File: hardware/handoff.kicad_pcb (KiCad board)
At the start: 2 copper layers, 40 x 62 mm, 65 parts, among them J1 BAT XH-2, J2 PAD JST-XH 2p, J3 LED JST-XH 4p / 5mm RGB, J5 CHG XH-2, J6 MOT 1x02 2.54, Q1 AO3400A, SW1 SS-12F23G5, SW2 TACT 6x6, U1 Raspberry Pi Pico 2 W, U2 MCP6292-E/MS

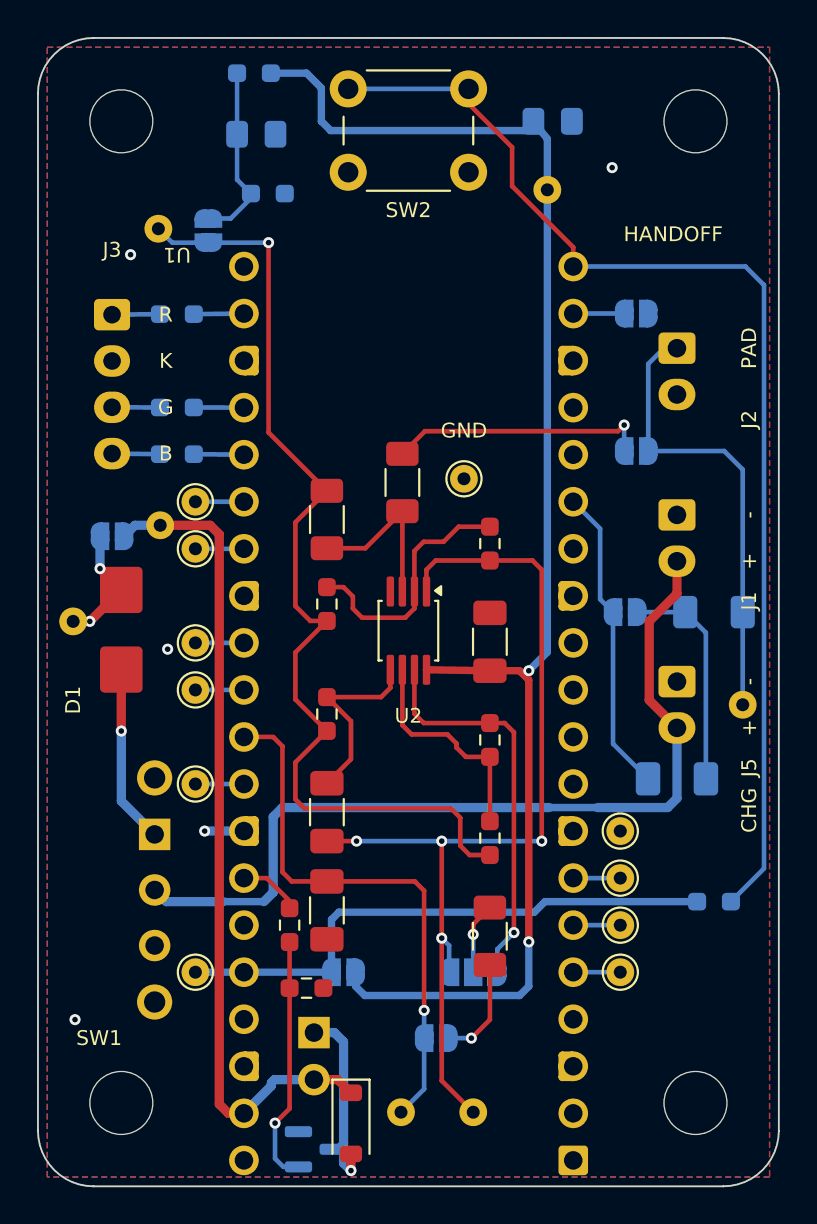
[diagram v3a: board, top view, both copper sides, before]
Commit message: Remove E1-E10, shrink the boss to 6 mm, and untangle the elbow
The board came in with 51 DRC errors. The previous session had been asked to
move D3 to the SS220F (SMB) like D1, and there was nowhere to put it: the SMB
took TP2 and TP3's spot beside J6, TP2 and TP3 were pushed out through two
gaps in the Pico's pin row to the little-finger wall, and there they landed on
top of the breakout pads. Four vias and two shorted pads to make room for one
diode. Take the space back instead of routing round the lack of it.

E1-E10 go. Ten through-hole pads on nets nothing uses, a column down each
wall, three of them (GP0, GP1, GND) sitting inside H4's boss for three
sessions. Gone from the schematic, the board, the DRU rule and the parts
list; the eight Pico pins they broke out are no-connect again, which is what
the sheet should say about a pin that goes nowhere. The Pico is socketed -
its own header is the breakout, and always was.

The boss is 6 mm, not 8. Six is enough to hold the 5 mm brass insert with a
wall round it; eight reached 4 mm in from two edges at once and was the only
reason each screw sat 4.5 mm from its corner. Hole position is derived now
rather than written out four times - BOSS_R + BOSS_EDGE from both edges - so
the boss keeps the same half-millimetre of wall and the screws move to
(3.5, 3.5) and its three mirrors. The footprint's name carries the diameter,
so a board built against a stale footprint cannot claim a keep-out it has
not got. The enclosure's printed bosses have to follow: 1 mm out
diagonally, 2 mm smaller.

Test pads are placed last now, into space the layout has already settled.
TP2 and TP3 sit ON their own net's existing lane, each replacing a via that
was there anyway, so neither costs a track, a corner or a pin-row crossing:
TP2 at (18.8, 54.0) on JP1's ADC0 pad row, TP3 at (21.0, 48.6) on OUT1's own
change of face into JP3. ADC0's lane moves to x 19.8 and OUT1's steps 0.8 mm
west to give TP3 its pad, which also has to clear JP3's pin-1 a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
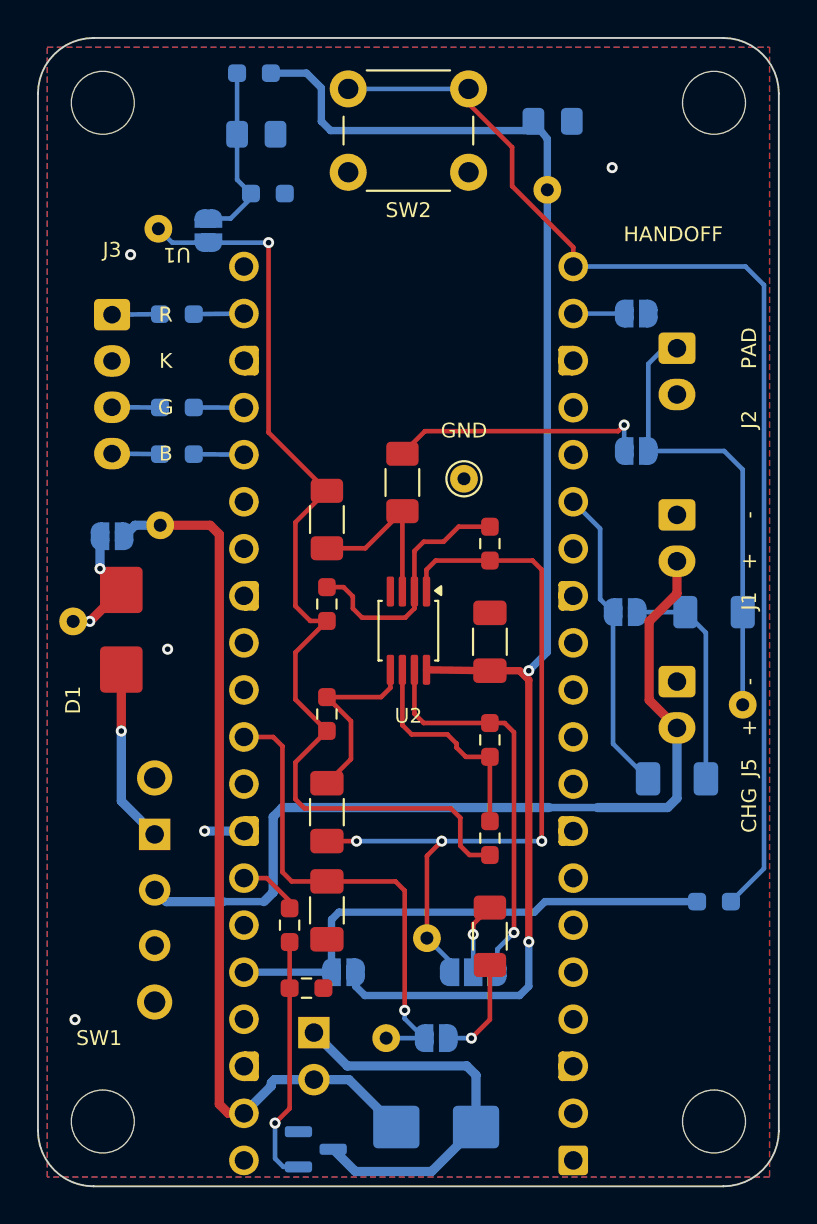
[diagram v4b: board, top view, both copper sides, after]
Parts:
- removed E1: 3V3 (pin 36), TestPoint:TestPoint_THTPad_D1.5mm_Drill0.7mm
- removed E10: GND (pin 8), TestPoint:TestPoint_THTPad_D1.5mm_Drill0.7mm
- removed E2: RUN (pin 30), TestPoint:TestPoint_THTPad_D1.5mm_Drill0.7mm
- removed E3: GP3 (pin 5), TestPoint:TestPoint_THTPad_D1.5mm_Drill0.7mm
- removed E4: GP22 (pin 29), TestPoint:TestPoint_THTPad_D1.5mm_Drill0.7mm
- removed E5: GP4 (pin 6), TestPoint:TestPoint_THTPad_D1.5mm_Drill0.7mm
- removed E6: GP5 (pin 7), TestPoint:TestPoint_THTPad_D1.5mm_Drill0.7mm
- removed E7: GP20 (pin 26), TestPoint:TestPoint_THTPad_D1.5mm_Drill0.7mm
- removed E8: GP21 (pin 27), TestPoint:TestPoint_THTPad_D1.5mm_Drill0.7mm
- removed E9: GP27 (pin 32), TestPoint:TestPoint_THTPad_D1.5mm_Drill0.7mm
- D3: value 1N5819W -> SS220F; footprint Diode_SMD:D_SOD-123 -> Diode_SMD:D_SMB; moved to B.Cu
- H1, H2, H3, H4: footprint handoff:MountingHole_3.4mm_M3_Boss8mm -> handoff:MountingHole_3.4mm_M3_Boss6mm
- moved TP3 9.73 mm to (21.0, 48.6)
- moved D3 4.60 mm to (21.5, 58.8), turned to 0 degrees
- moved TP2 4.08 mm to (18.8, 54.0)
- moved H1 1.41 mm to (3.50, 3.50)
- moved H2 1.41 mm to (36.5, 3.50)
- moved H3 1.41 mm to (3.50, 58.5)
- moved H4 1.41 mm to (36.5, 58.5)
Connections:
- U1 pad 26: /GP20 -> unconnected-(U1-GPIO20-Pad26)
- U1 pad 27: /GP21 -> unconnected-(U1-GPIO21-Pad27)
- U1 pad 29: /GP22 -> unconnected-(U1-GPIO22-Pad29)
- U1 pad 30: /RUN -> unconnected-(U1-RUN-Pad30)
- U1 pad 32: /GP27_ADC1 -> unconnected-(U1-GPIO27_ADC1-Pad32)
- U1 pad 5: /GP3 -> unconnected-(U1-GPIO3-Pad5)
- U1 pad 6: /GP4 -> unconnected-(U1-GPIO4-Pad6)
- U1 pad 7: /GP5 -> unconnected-(U1-GPIO5-Pad7)
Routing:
- net /MOT_SW: track 10.2 -> 21.7 mm, vias 1 -> 0
- net /OUT1: track 51.4 -> 42.0 mm, vias 4 -> 3
- net VSYS: track 44.8 -> 48.0 mm
- net /ADC0: track 29.6 -> 26.5 mm
- net +3V3: track 30.3 -> 27.7 mm
- net /RUN: track 2.62 -> 0.00 mm
- net /GP27_ADC1: track 2.62 -> 0.00 mm
- net /GP22: track 2.62 -> 0.00 mm
- net /GP21: track 2.62 -> 0.00 mm
- net /GP20: track 2.62 -> 0.00 mm
- net /GP5: track 2.30 -> 0.00 mm
- net /GP4: track 2.30 -> 0.00 mm
- net /GP3: track 2.30 -> 0.00 mm
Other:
- board text added: "HANDOFF rev A - 2 layer, 40 x 62 mm, 1.6 mm FR-4, 1 oz Cu, HASL lead-free, green mask, white silk. Min track/space 0.25/0.2 (design), 0.15 (fab floor). Min solder-mask dam 0.1. Drills 0.3 / 0.7 / 0.95 / 1.0 / 1.1 / 1.15 PTH and 3.4 NPTH - see build/drills.md. H1-H4 3.4 mm unplated, each inside a 6 mm enclosure boss."
- board text removed: "HANDOFF rev A - 2 layer, 40 x 62 mm, 1.6 mm FR-4, 1 oz Cu, HASL lead-free, green mask, white silk. Min track/space 0.25/0.2 (design), 0.15 (fab floor). Min solder-mask dam 0.1. Drills 0.3 / 0.7 / 0.95 / 1.0 / 1.1 / 1.15 PTH and 3.4 NPTH - see build/drills.md. H1-H4 3.4 mm unplated, each inside an 8 mm enclosure boss."

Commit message: Move every passive to 0603 and D1/D3 to the PMEG3020ER-TP (SOD-123FL)
The 12 Sep order: R1-R3, R9, C1-C3, C6 from 1206 and C4/C5 from 0805 to 0603;
both Schottkys from the SS220F (SMB) to the Tech Public PMEG3020ER-TP, 40 V
2 A, in SOD-123FL - not the Nexperia part of the same number. KiCad has no
SOD-123FL, so gen_sod123fl_footprint.py writes one from the outline drawing
and proves it on a test board. No net changes; EXPECTED_NETS is untouched.

What the pad shift broke, all found by the checks: C1 landed on the VREF bus
it used to straddle (origin now on the bus, OUT1's corridor derived from it);
the AFE pocket's exit between R3's pads closed under VREF's 45 (VREF enters
R3.2 flat now); C6 could not straddle BAT+ (stands under JP2 instead); R3's
old pad centre became a bare right angle. R2 moves 1 mm toward U2 and the
1 MOhm island is 8.5 mm, written entirely against pads. Both diodes needed no
route change. Pours: top 1611 -> 1630 mm2, bottom 1155 -> 1179. D1's cathode
bar is on silk again.

gen_bom.py now derives bom.csv's Package column instead of it being typed in;
gen_schematic.py calls it. README: parts table, D1 deviation (0.4 V, and the
GP29 correction now agrees with it), the 10 uF paragraph, one-package
statement, and a session log with the C0G / 25 V / R2-R3 ESD reasoning.

Co-Authored-By: Claude Opus 5 <noreply@anthropic.com>
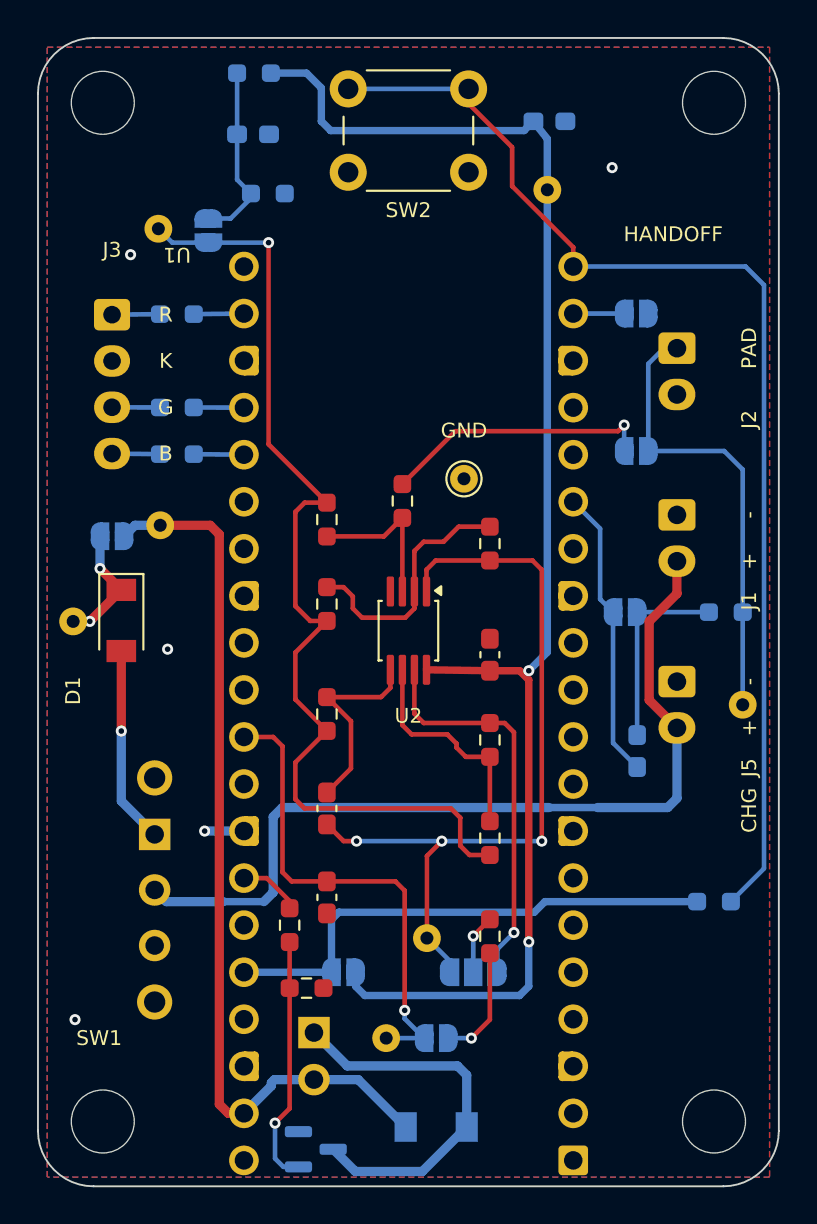
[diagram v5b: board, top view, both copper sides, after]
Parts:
- C1, C2, C3, C6: footprint Capacitor_SMD:C_1206_3216Metric_Pad1.33x1.80mm_HandSolder -> Capacitor_SMD:C_0603_1608Metric_Pad1.08x0.95mm_HandSolder
- C4, C5: value 10uF 100V -> 10uF 25V; footprint Capacitor_SMD:C_0805_2012Metric_Pad1.18x1.45mm_HandSolder -> Capacitor_SMD:C_0603_1608Metric_Pad1.08x0.95mm_HandSolder
- D1, D3: value SS220F -> PMEG3020ER-TP; footprint Diode_SMD:D_SMB -> handoff:D_SOD-123FL
- R1, R2, R3, R9: footprint Resistor_SMD:R_1206_3216Metric_Pad1.30x1.75mm_HandSolder -> Resistor_SMD:R_0603_1608Metric_Pad0.98x0.95mm_HandSolder
- moved C6 2.62 mm to (32.4, 38.5), turned to 90 degrees
- moved R2 1.00 mm to (19.7, 25.0)
- moved C3 0.70 mm to (24.4, 33.3)
- moved C2 0.70 mm to (15.6, 46.4)
- moved R1 0.64 mm to (37.1, 31.0)
- moved D1 0.50 mm to (4.50, 31.4)
- moved C1 0.20 mm to (15.6, 41.6)
- moved C5 0.18 mm to (27.6, 4.50)
- moved C4 0.17 mm to (11.6, 5.20)
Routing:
- net Net-(JP2-B): track 12.1 -> 10.5 mm
- net /SW_OUT: track 9.65 -> 10.6 mm
- net /MOT_SW: track 21.7 -> 20.7 mm
- net /GP11_TX: track 16.6 -> 15.8 mm
- net Net-(U2A-+): track 9.24 -> 8.46 mm
- net VREF: track 54.3 -> 55.0 mm
- net Net-(JP7-B): track 14.0 -> 14.7 mm
- net Net-(JP3-C): track 3.86 -> 3.23 mm
- net Net-(JP1-A): track 5.61 -> 6.25 mm
- net Net-(U2B-+): track 10.3 -> 10.8 mm

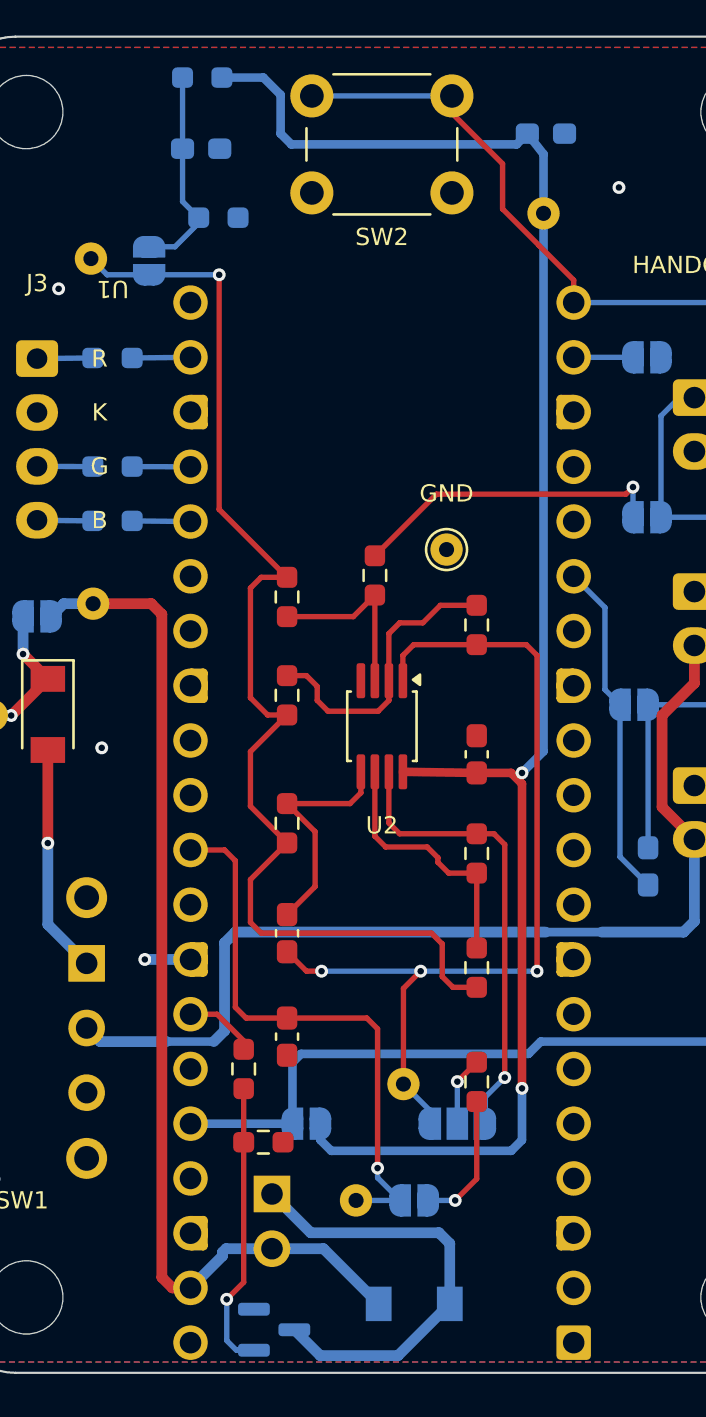
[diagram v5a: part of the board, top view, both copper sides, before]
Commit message: Tidy eleven routes: one leg and one 45, no jogs, stubs or off-45 legs
Pin 2's north escape and pin 6's run to R7.1 were staircases; pin 2's FB1
was a U-turn round pin 4. Each is now a straight leg and one 45 onto the
resistor's pad row. FB1's 45 lands on R5.1's row at x 16.9, not on the pad
and not from pin 7's column - both close the U2-body pour's only exit.

Also: OUT1 leaves pin 1 with a 45; VREF leaves R8.2 with one 45 to the bus;
ADC0 into pin 31, AGND out of pin 33 and GP28 into R16 are true 45s; the
0.25 mm stub at R11.1, 0.34 mm at J6 and 0.45 mm at ADC0's via are gone
(ADC0_VIA sits where the 45 into JP1.2 starts); AFE_3V3's 52-degree leg into
C5.1 is a 45; BTN loses a collinear point. 18 segments fewer, no lane moved.
DRC 0, shorts 0, parity 0, unrouted 0.

Co-Authored-By: Claude Opus 5 <noreply@anthropic.com>
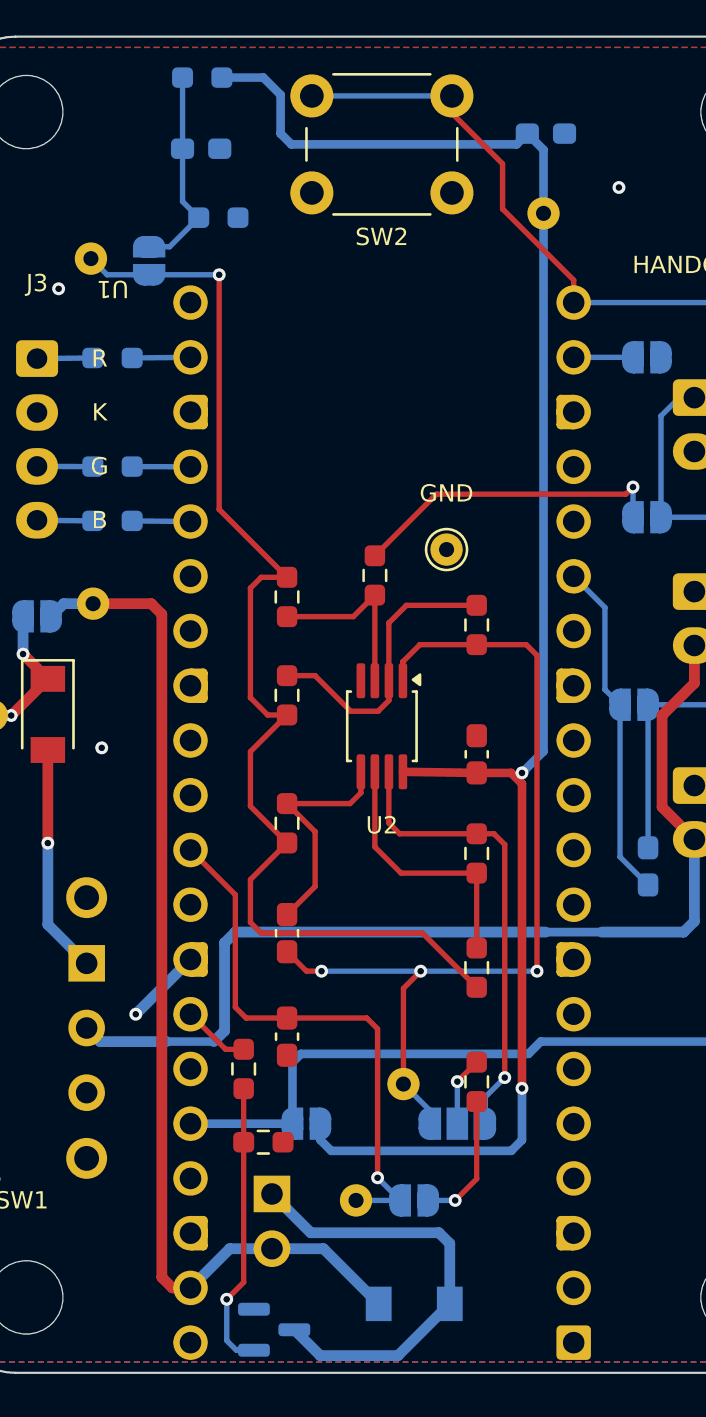
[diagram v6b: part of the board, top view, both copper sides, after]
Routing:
- net GND: track 2.12 -> 3.59 mm
- net /ADC0: track 26.5 -> 25.6 mm
- net VREF: track 55.0 -> 54.1 mm
